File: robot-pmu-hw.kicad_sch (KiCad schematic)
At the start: 0 parts

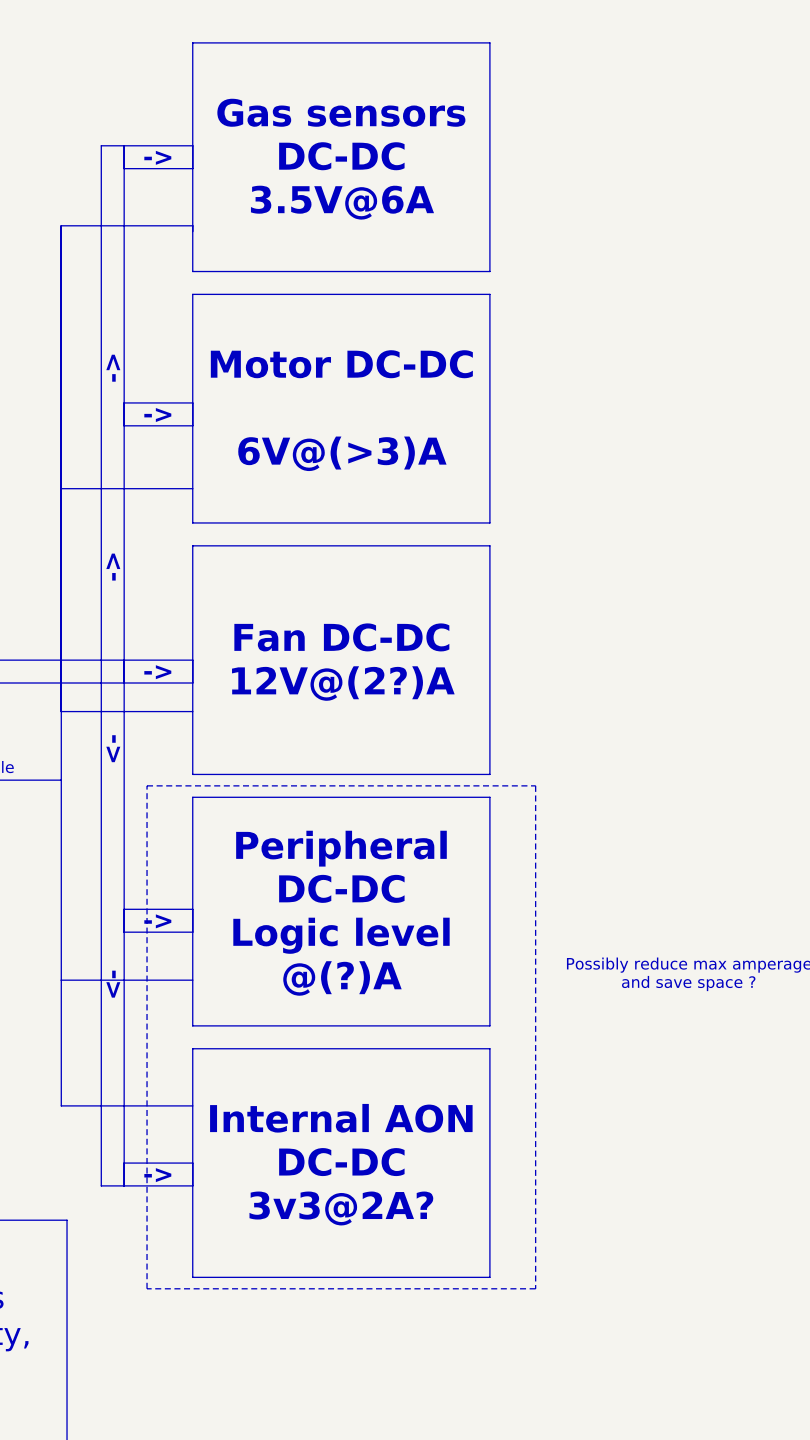
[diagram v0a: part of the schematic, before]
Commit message: Added DC-DC converters
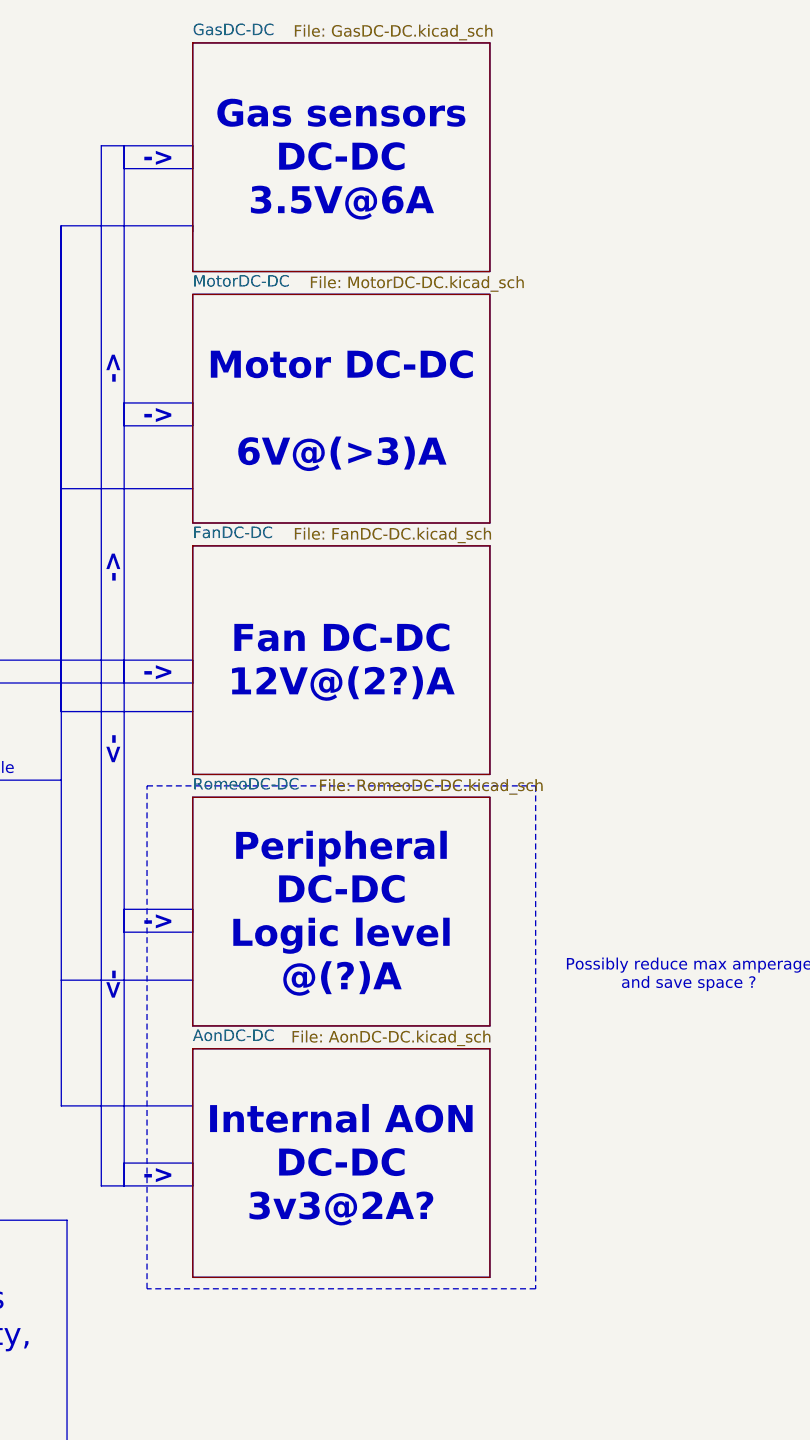
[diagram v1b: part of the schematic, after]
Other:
- added sheet AonDC-DC (AonDC-DC.kicad_sch)
- added sheet FanDC-DC (FanDC-DC.kicad_sch)
- added sheet GasDC-DC (GasDC-DC.kicad_sch)
- added sheet MotorDC-DC (MotorDC-DC.kicad_sch)
- added sheet RomeoDC-DC (RomeoDC-DC.kicad_sch)
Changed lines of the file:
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@@
+		)
+	)
+	(sheet
+		(at 236.22 95.25)
+		(size 33.02 25.4)
+		(exclude_from_sim no)
+		(in_bom yes)
+		(on_board yes)
+		(dnp no)
+		(stroke
+			(width 0.1524)
+			(type solid)
+		)
+		(fill
+			(color 0 0 0 0.0000)
+		)
+		(property "Sheetname" "MotorDC-DC"
+			(at 236.22 94.5384 0)
+			(effects
+				(font
+					(size 1.27 1.27)
+				)
+				(justify left bottom)
+			)
+		)
+		(property "Sheetfile" "MotorDC-DC.kicad_sch"
+			(at 249.174 93.218 0)
+			(effects
+				(font
+					(size 1.27 1.27)
+				)
+				(justify left top)
+			)
+		)
+		(instances
+			(project "robot-pmu-hw"
+				(path "/ca7f4c4c-3c96-472a-b66f-ec124f8cf9b5"
+					(page "3")
+				)
+			)
+		)
+	)
+	(sheet
+		(at 236.22 151.13)
+		(size 33.02 25.4)
+		(exclude_from_sim no)
+		(in_bom yes)
+		(on_board yes)
+		(dnp no)
+		(stroke
+			(width 0.1524)
+			(type solid)
+		)
+		(fill
+			(color 0 0 0 0.0000)
+		)
+		(property "Sheetname" "RomeoDC-DC"
+			(at 236.22 150.4184 0)
+			(effects
+				(font
+					(size 1.27 1.27)
+				)
+				(justify left bottom)
+			)
+		)
+		(property "Sheetfile" "RomeoDC-DC.kicad_sch"
+			(at 250.19 149.098 0)
+			(effects
+				(font
+					(size 1.27 1.27)
+				)
+				(justify left top)
+			)
+		)
+		(instances
+			(project "robot-pmu-hw"
+				(path "/ca7f4c4c-3c96-472a-b66f-ec124f8cf9b5"
+					(page "5")
+				)
+			)
+		)
+	)
+	(sheet
+		(at 236.22 123.19)
+		(size 33.02 25.4)
+		(exclude_from_sim no)
+		(in_bom yes)
+		(on_board yes)
+		(dnp no)
+		(stroke
+			(width 0.1524)
+			(type solid)
+		)
+		(fill
+			(color 0 0 0 0.0000)
+		)
+		(property "Sheetname" "FanDC-DC"
+			(at 236.22 122.4784 0)
+			(effects
+				(font
+					(size 1.27 1.27)
+				)
+				(justify left bottom)
+			)
+		)
+		(property "Sheetfile" "FanDC-DC.kicad_sch"
+			(at 247.396 121.158 0)
+			(effects
+				(font
+					(size 1.27 1.27)
+				)
+				(justify left top)
+			)
+		)
+		(instances
+			(project "robot-pmu-hw"
+				(path "/ca7f4c4c-3c96-472a-b66f-ec124f8cf9b5"
+					(page "4")
+				)
+			)
+		)
+	)
+	(sheet
+		(at 236.22 67.31)
+		(size 33.02 25.4)
+		(exclude_from_sim no)
+		(in_bom yes)
+		(on_board yes)
+		(dnp no)
+		(stroke
+			(width 0.1524)
+			(type solid)
+		)
+		(fill
+			(color 0 0 0 0.0000)
+		)
+		(property "Sheetname" "GasDC-DC"
+			(at 236.22 66.5984 0)
+			(effects
+				(font
+					(size 1.27 1.27)
+				)
+				(justify left bottom)
+			)
+		)
+		(property "Sheetfile" "GasDC-DC.kicad_sch"
+			(at 247.396 65.278 0)
+			(effects
+				(font
+					(size 1.27 1.27)
+				)
+				(justify left top)
+			)
+		)
+		(instances
+			(project "robot-pmu-hw"
+				(path "/ca7f4c4c-3c96-472a-b66f-ec124f8cf9b5"
+					(page "2")
+				)
+			)
+		)
+	)
+	(sheet
+		(at 236.22 179.07)
+		(size 33.02 25.4)
+		(exclude_from_sim no)
+		(in_bom yes)
+		(on_board yes)
+		(dnp no)
+		(stroke
+			(width 0.1524)
+			(type solid)
+		)
+		(fill
+			(color 0 0 0 0.0000)
+		)
+		(property "Sheetname" "AonDC-DC"
+			(at 236.22 178.3584 0)
+			(effects
+				(font
+					(size 1.27 1.27)
+				)
+				(justify left bottom)
+			)
+		)
+		(property "Sheetfile" "AonDC-DC.kicad_sch"
+			(at 247.142 177.038 0)
+			(effects
+				(font
+					(size 1.27 1.27)
+				)
+				(justify left top)
+			)
+		)
+		(instances
+			(project "robot-pmu-hw"
+				(path "/ca7f4c4c-3c96-472a-b66f-ec124f8cf9b5"
+					(page "6")
+				)
+			)
 		)
 	)
